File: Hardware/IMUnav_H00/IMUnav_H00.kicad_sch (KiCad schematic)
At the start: 39 parts, among them J1 Conn_01x03_Pin, J2 Conn_01x03_Pin, J3 Conn_01x03_Pin, J4 Conn_01x03_Pin, J5 Conn_01x03_Pin, J6 Conn_01x03_Pin, U1 STM32F446VETx, X1 SX5M24.000M20F30TNN

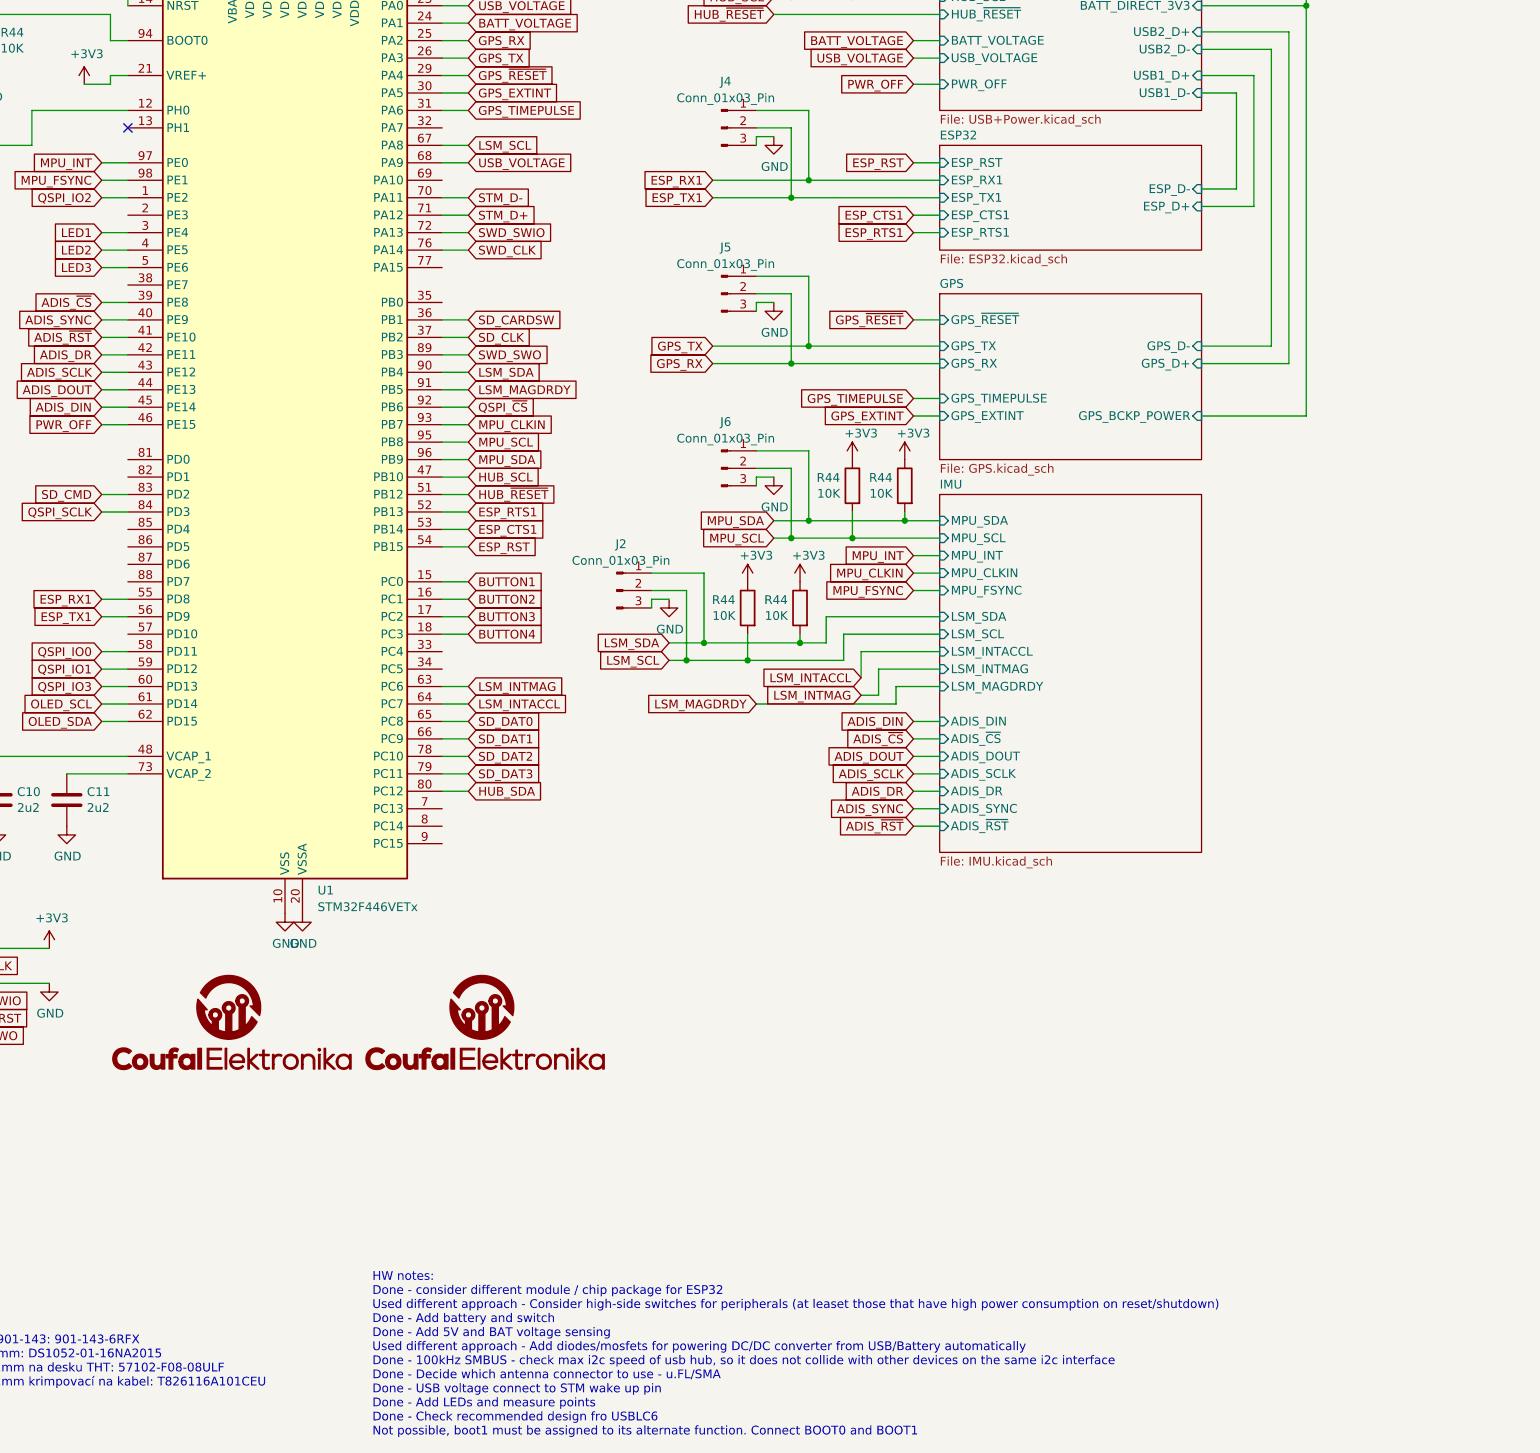
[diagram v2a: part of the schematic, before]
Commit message: Changed LSM303C to LSM303AGR
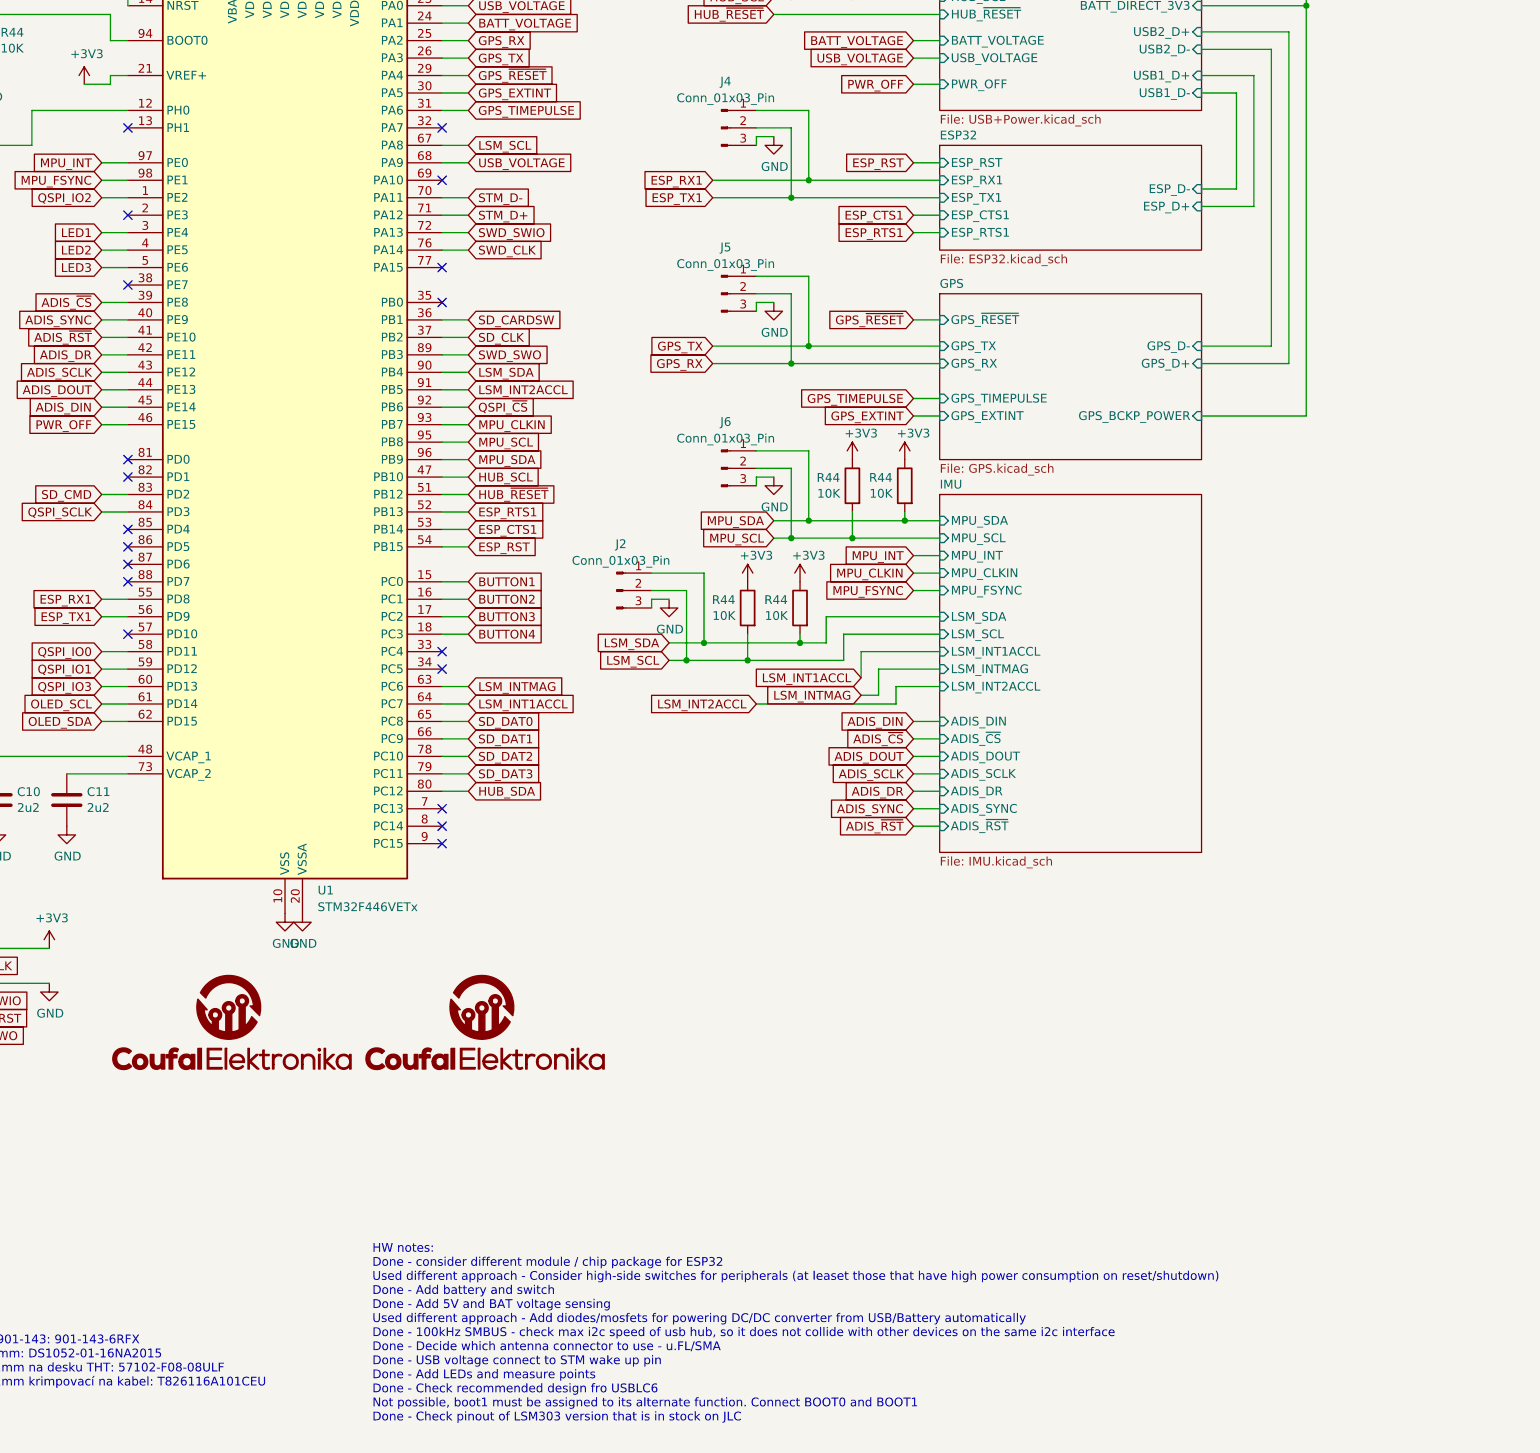
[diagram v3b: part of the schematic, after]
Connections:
- net LSM_INTACCL renamed LSM_INT1ACCL
- net LSM_MAGDRDY renamed LSM_INT2ACCL
- no-connect marks 3 -> 21
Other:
- sheet IMU ports: added LSM_INT1ACCL, LSM_INT2ACCL; removed LSM_INTACCL, LSM_MAGDRDY
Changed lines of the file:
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@@
   (junction (at 73.66 25.4) (diameter 0) (color 0 0 0 0)
   )
+  (no_connect (at 106.68 123.19))
+  (no_connect (at 152.4 161.29))
+  (no_connect (at 152.4 156.21))
+  (no_connect (at 106.68 105.41))
+  (no_connect (at 106.68 69.85))
+  (no_connect (at 152.4 64.77))
+  (no_connect (at 106.68 118.11))
+  (no_connect (at 152.4 77.47))
+  (no_connect (at 106.68 130.81))
+  (no_connect (at 106.68 115.57))
+  (no_connect (at 106.68 120.65))
   (no_connect (at 106.68 57.15))
   (no_connect (at 270.51 27.94))
+  (no_connect (at 152.4 57.15))
+  (no_connect (at 152.4 82.55))
+  (no_connect (at 106.68 107.95))
   (no_connect (at 270.51 25.4))
+  (no_connect (at 152.4 133.35))
+  (no_connect (at 152.4 135.89))
+  (no_connect (at 152.4 158.75))
+  (no_connect (at 106.68 80.01))
   (wire (pts (xy 78.74 93.98) (xy 71.12 93.98))
     (stroke (width 0) (type default))
@@
     (stroke (width 0) (type default))
   )
-  (text "HW notes:\nDone - consider different module / chip package for ESP32\nUsed different approach - Consider high-side switches for peripherals (at leaset those that have high power consumption on reset/shutdown)\nDone - Add battery and switch\nDone - Add 5V and BAT voltage sensing\nUsed different approach - Add diodes/mosfets for powering DC/DC converter from USB/Battery automatically\nDone - 100kHz SMBUS - check max i2c speed of usb hub, so it does not collide with other devices on the same i2c interface\nDone - Decide which antenna connector to use - u.FL/SMA\nDone - USB voltage connect to STM wake up pin\nDone - Add LEDs and measure points\nDone - Check recommended design fro USBLC6\nNot possible, boot1 must be assigned to its alternate function. Connect BOOT0 and BOOT1\n"
+  (text "HW notes:\nDone - consider different module / chip package for ESP32\nUsed different approach - Consider high-side switches for peripherals (at leaset those that have high power consumption on reset/shutdown)\nDone - Add battery and switch\nDone - Add 5V and BAT voltage sensing\nUsed different approach - Add diodes/mosfets for powering DC/DC converter from USB/Battery automatically\nDone - 100kHz SMBUS - check max i2c speed of usb hub, so it does not collide with other devices on the same i2c interface\nDone - Decide which antenna connector to use - u.FL/SMA\nDone - USB voltage connect to STM wake up pin\nDone - Add LEDs and measure points\nDone - Check recommended design fro USBLC6\nNot possible, boot1 must be assigned to its alternate function. Connect BOOT0 and BOOT1\nDone - Check pinout of LSM303 version that is in stock on JLC\n\n"
     (at 142.24 247.65 0)
     (effects (font (size 1.27 1.27)) (justify left bottom))
@@
     )
   )
-  (global_label "LSM_MAGDRDY" (shape input) (at 198.12 140.97 180) (fields_autoplaced)
+  (global_label "LSM_INT2ACCL" (shape input) (at 198.12 140.97 180) (fields_autoplaced)
     (effects (font (size 1.27 1.27)) (justify right))
-    (property "Intersheetrefs" "${INTERSHEET_REFS}" (at 181.7696 140.97 0)
+    (property "Intersheetrefs" "${INTERSHEET_REFS}" (at 181.7091 140.97 0)
       (effects (font (size 1.27 1.27)) (justify right) hide)
     )
@@
     )
   )
+  (global_label "LSM_INT2ACCL" (shape input) (at 156.21 95.25 0) (fields_autoplaced)
+    (effects (font (size 1.27 1.27)) (justify left))
+    (property "Intersheetrefs" "${INTERSHEET_REFS}" (at 172.6209 95.25 0)
+      (effects (font (size 1.27 1.27)) (justify left) hide)
+    )
+  )
   (global_label "SWD_CLK" (shape input) (at 80.01 179.07 0) (fields_autoplaced)
     (effects (font (size 1.27 1.27)) (justify left))
@@
     )
   )
+  (global_label "LSM_INT1ACCL" (shape input) (at 156.21 140.97 0) (fields_autoplaced)
+    (effects (font (size 1.27 1.27)) (justify left))
+    (property "Intersheetrefs" "${INTERSHEET_REFS}" (at 172.6209 140.97 0)
+      (effects (font (size 1.27 1.27)) (justify left) hide)
+    )
+  )
   (global_label "ESP_CTS1" (shape input) (at 156.21 115.57 0) (fields_autoplaced)
     (effects (font (size 1.27 1.27)) (justify left))
@@
     )
   )
-  (global_label "LSM_MAGDRDY" (shape input) (at 156.21 95.25 0) (fields_autoplaced)
-    (effects (font (size 1.27 1.27)) (justify left))
-    (property "Intersheetrefs" "${INTERSHEET_REFS}" (at 172.5604 95.25 0)
-      (effects (font (size 1.27 1.27)) (justify left) hide)
-    )
-  )
   (global_label "MPU_CLKIN" (shape input) (at 220.98 121.92 180) (fields_autoplaced)
     (effects (font (size 1.27 1.27)) (justify right))
@@
     )
   )
-  (global_label "LSM_INTACCL" (shape input) (at 156.21 140.97 0) (fields_autoplaced)
-    (effects (font (size 1.27 1.27)) (justify left))
-    (property "Intersheetrefs" "${INTERSHEET_REFS}" (at 171.4114 140.97 0)
-      (effects (font (size 1.27 1.27)) (justify left) hide)
-    )
-  )
   (global_label "QSPI_IO3" (shape input) (at 102.87 138.43 180) (fields_autoplaced)
     (effects (font (size 1.27 1.27)) (justify right))
@@
     )
   )
-  (global_label "LSM_INTACCL" (shape input) (at 213.36 137.16 180) (fields_autoplaced)
+  (global_label "LSM_INT1ACCL" (shape input) (at 213.36 137.16 180) (fields_autoplaced)
     (effects (font (size 1.27 1.27)) (justify right))
-    (property "Intersheetrefs" "${INTERSHEET_REFS}" (at 198.1586 137.16 0)
+    (property "Intersheetrefs" "${INTERSHEET_REFS}" (at 196.9491 137.16 0)
       (effects (font (size 1.27 1.27)) (justify right) hide)
     )
@@
   (sheet (at 224.79 110.49) (size 38.1 52.07) (fields_autoplaced)
     (stroke (width 0.1524) (type solid))
-    (fill (color 0 0 0 0.0000))
+    (fill (color 194 194 194 1.0000))
     (property "Sheetname" "IMU" (at 224.79 109.7784 0)
       (effects (font (size 1.27 1.27)) (justify left bottom))
@@
       (effects (font (size 1.27 1.27)) (justify left))
     )
-    (pin "LSM_INTACCL" input (at 224.79 133.35 180)
-      (effects (font (size 1.27 1.27)) (justify left))
-    )
     (pin "LSM_INTMAG" input (at 224.79 135.89 180)
       (effects (font (size 1.27 1.27)) (justify left))
     )
-    (pin "LSM_MAGDRDY" input (at 224.79 138.43 180)
-      (effects (font (size 1.27 1.27)) (justify left))
-    )
     (pin "ADIS_DIN" input (at 224.79 143.51 180)
       (effects (font (size 1.27 1.27)) (justify left))
@@
       (effects (font (size 1.27 1.27)) (justify left))
     )
+    (pin "LSM_INT1ACCL" input (at 224.79 133.35 180)
+      (effects (font (size 1.27 1.27)) (justify left))
+    )
+    (pin "LSM_INT2ACCL" input (at 224.79 138.43 180)
+      (effects (font (size 1.27 1.27)) (justify left))
+    )
     (instances
       (project "IMUnav_H00"
@@
   (sheet (at 224.79 81.28) (size 38.1 24.13) (fields_autoplaced)
     (stroke (width 0.1524) (type solid))
-    (fill (color 0 0 0 0.0000))
+    (fill (color 194 194 194 1.0000))
     (property "Sheetname" "GPS" (at 224.79 80.5684 0)
       (effects (font (size 1.27 1.27)) (justify left bottom))
@@
   (sheet (at 224.79 22.86) (size 38.1 31.75) (fields_autoplaced)
     (stroke (width 0) (type solid))
-    (fill (color 0 0 0 0.0000))
+    (fill (color 194 194 194 1.0000))
     (property "Sheetname" "USB+Power" (at 224.79 22.1484 0)
       (effects (font (size 1.27 1.27)) (justify left bottom))
@@
   (sheet (at 15.24 43.18) (size 38.1 45.72) (fields_autoplaced)
     (stroke (width 0.1524) (type solid))
-    (fill (color 0 0 0 0.0000))
+    (fill (color 194 194 194 1.0000))
     (property "Sheetname" "Memory" (at 15.24 42.4684 0)
       (effects (font (size 1.27 1.27)) (justify left bottom))
@@
   (sheet (at 13.97 101.6) (size 38.1 30.48) (fields_autoplaced)
     (stroke (width 0.1524) (type solid))
-    (fill (color 0 0 0 0.0000))
+    (fill (color 194 194 194 1.0000))
     (property "Sheetname" "User" (at 13.97 100.8884 0)
       (effects (font (size 1.27 1.27)) (justify left bottom))
@@
   (sheet (at 224.79 59.69) (size 38.1 15.24) (fields_autoplaced)
     (stroke (width 0.1524) (type solid))
-    (fill (color 0 0 0 0.0000))
+    (fill (color 194 194 194 1.0000))
     (property "Sheetname" "ESP32" (at 224.79 58.9784 0)
       (effects (font (size 1.27 1.27)) (justify left bottom))

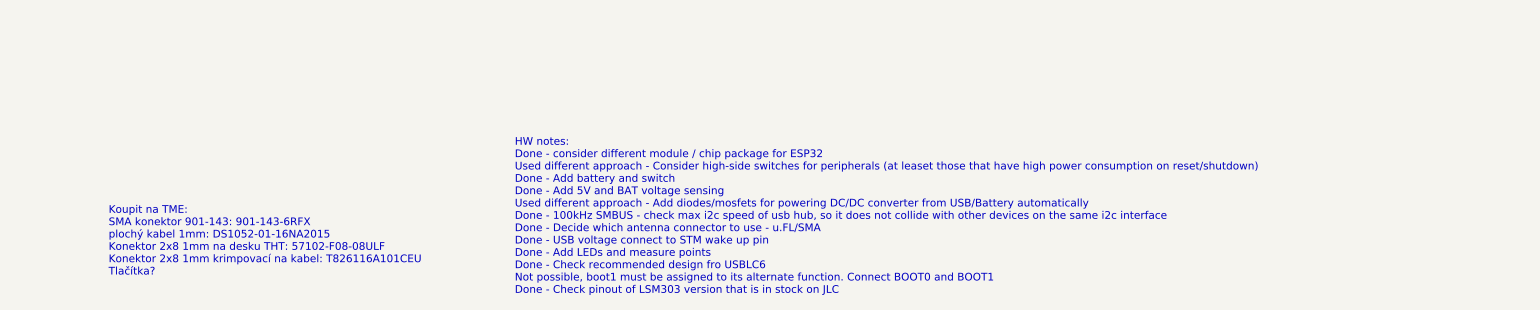
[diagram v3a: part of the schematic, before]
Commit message: PCB layout - BGA fanout, GPS and USB hub
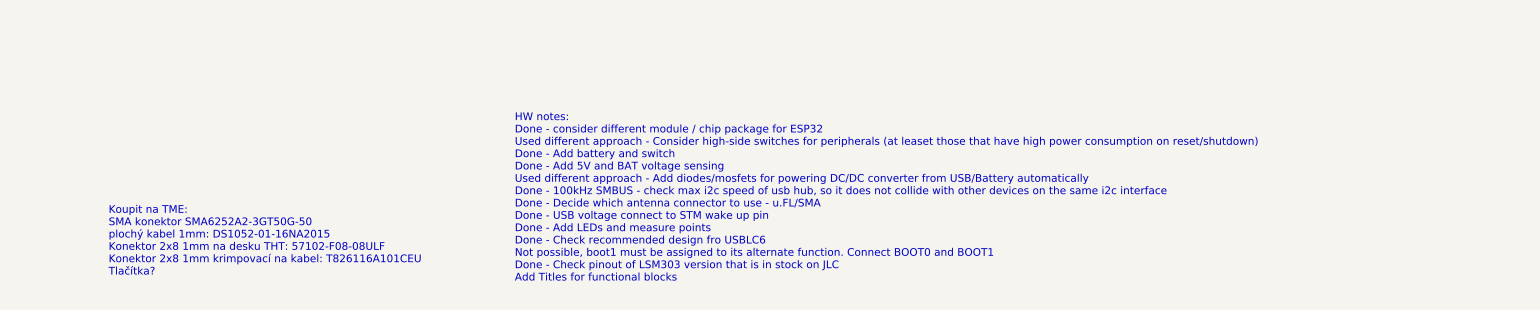
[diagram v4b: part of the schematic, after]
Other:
- note added: "Koupit na TME: SMA konektor SMA6252A2-3GT50G-50 plochý kabel 1mm: DS1052-01-16NA2015 Konektor 2x8 1mm na desku THT: 57102-F08-08ULF Konektor 2x8 1mm krimpovací na kabel: T826116A101CEU Tlačítka?"
- note removed: "Koupit na TME: SMA konektor 901-143: 901-143-6RFX plochý kabel 1mm: DS1052-01-16NA2015 Konektor 2x8 1mm na desku THT: 57102-F08-08ULF Konektor 2x8 1mm krimpovací na kabel: T826116A101CEU Tlačítka?"
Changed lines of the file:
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@@
     (stroke (width 0) (type default))
   )
-  (text "HW notes:\nDone - consider different module / chip package for ESP32\nUsed different approach - Consider high-side switches for peripherals (at leaset those that have high power consumption on reset/shutdown)\nDone - Add battery and switch\nDone - Add 5V and BAT voltage sensing\nUsed different approach - Add diodes/mosfets for powering DC/DC converter from USB/Battery automatically\nDone - 100kHz SMBUS - check max i2c speed of usb hub, so it does not collide with other devices on the same i2c interface\nDone - Decide which antenna connector to use - u.FL/SMA\nDone - USB voltage connect to STM wake up pin\nDone - Add LEDs and measure points\nDone - Check recommended design fro USBLC6\nNot possible, boot1 must be assigned to its alternate function. Connect BOOT0 and BOOT1\nDone - Check pinout of LSM303 version that is in stock on JLC\n\n"
+  (text "HW notes:\nDone - consider different module / chip package for ESP32\nUsed different approach - Consider high-side switches for peripherals (at leaset those that have high power consumption on reset/shutdown)\nDone - Add battery and switch\nDone - Add 5V and BAT voltage sensing\nUsed different approach - Add diodes/mosfets for powering DC/DC converter from USB/Battery automatically\nDone - 100kHz SMBUS - check max i2c speed of usb hub, so it does not collide with other devices on the same i2c interface\nDone - Decide which antenna connector to use - u.FL/SMA\nDone - USB voltage connect to STM wake up pin\nDone - Add LEDs and measure points\nDone - Check recommended design fro USBLC6\nNot possible, boot1 must be assigned to its alternate function. Connect BOOT0 and BOOT1\nDone - Check pinout of LSM303 version that is in stock on JLC\nAdd Titles for functional blocks\n\n\n"
     (at 142.24 247.65 0)
     (effects (font (size 1.27 1.27)) (justify left bottom))
   )
-  (text "Koupit na TME:\nSMA konektor 901-143: 901-143-6RFX\nplochý kabel 1mm: DS1052-01-16NA2015\nKonektor 2x8 1mm na desku THT: 57102-F08-08ULF\nKonektor 2x8 1mm krimpovací na kabel: T826116A101CEU\nTlačítka?\n"
+  (text "Koupit na TME:\nSMA konektor SMA6252A2-3GT50G-50\nplochý kabel 1mm: DS1052-01-16NA2015\nKonektor 2x8 1mm na desku THT: 57102-F08-08ULF\nKonektor 2x8 1mm krimpovací na kabel: T826116A101CEU\nTlačítka?\n"
     (at 74.93 242.57 0)
     (effects (font (size 1.27 1.27)) (justify left bottom))
